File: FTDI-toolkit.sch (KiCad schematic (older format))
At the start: 122 parts, among them IC1 TLV70033, IC13 74HC00BQ, IC15 TS5A3359, IC2 TLV70018, IC3 TS5A3359, J1 12401598E4_2A, J2 2X05, J3 2X08, J6 61300411121, Q1 NX3008CBKV, Q2 NX3008CBKV, SW1_A1 1X03, SW1_B1 1X03, SW2_A1 1X03, SW2_B1 1X03, U1 FT2232H-56Q, U10 74LVC2T45GT, U11 NTS0302JKZ, U2 SN74LVC1T45DRLR, U3 SN74LVC1T45DRLR, U4 TXB0104RUT, U5 74LVC2T45GT, U6 74LVC2T45GT, U7 74LVC2T45GT, U8 SN74LVC1T45DRLR, U9 SN74LVC1T45DRLR, Y1 ASFLMB-12.000MHZ-LC-T

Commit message: Move separation resistors for SWD and I2C switches
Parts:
- added C16, C34, C35: C_100n_0402_16V, antmicro-footprints:0402-cap, symbol antmicroCapacitors0402:C_100n_0402_16V
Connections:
- wire segments 482 -> 480
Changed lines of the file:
@@
 Wire Wire Line
 	2200 5800 2200 5750
-Connection ~ 2200 5750
-Wire Wire Line
-	2200 5750 2550 5750
 Wire Wire Line
 	5400 9000 6300 9000
@@
 Text GLabel 5500 3750 1    50   Input ~ 0
 5V_USB
-Connection ~ 2550 5750
 Wire Wire Line
 	2950 9400 3800 9400
@@
 $EndComp
 Wire Wire Line
-	2550 5750 3550 5750
+	2550 5750 2900 5750
 Wire Wire Line
 	2550 6550 2550 6450
@@
 U 1 1 61826E03
 P 14050 13000
-F 0 "U7" H 13800 13400 60  0000 C CNN
-F 1 "74LVC2T45GT" H 14050 13300 60  0000 C CNN
+F 0 "U7" H 13700 13450 60  0000 C CNN
+F 1 "74LVC2T45GT" H 13950 13350 60  0000 C CNN
 F 2 "antmicro-footprints:PSON50P100X195X50-8N" H 14250 13200 60  0001 L CNN
 F 3 "http://www.farnell.com/datasheets/2787504.pdf" H 14250 13300 60  0001 L CNN
@@
 Wire Wire Line
 	13200 10250 13950 10250
-Text GLabel 13450 12750 0    50   Input ~ 0
-3V3_FT
 Wire Wire Line
-	13450 12750 13550 12750
+	13450 12700 13550 12700
 Wire Wire Line
-	13550 12750 13550 12900
+	13550 12700 13550 12900
 Wire Wire Line
 	13550 13200 13750 13200
@@
 BDBUS1
 Wire Wire Line
-	14600 13100 14600 13500
+	14650 13100 14650 13500
 Wire Wire Line
-	14600 13500 13950 13500
-Wire Wire Line
-	14350 13100 14600 13100
+	14350 13100 14650 13100
 Text Label 13500 13500 2    60   ~ 0
 BDBUS2
 Wire Wire Line
-	14350 13000 14600 13000
-Wire Wire Line
 	14800 13100 14800 12900
 Wire Wire Line
 	14800 13100 15350 13100
 Wire Wire Line
-	14600 12750 13650 12750
+	14650 12700 13650 12700
 Wire Wire Line
-	13650 12750 13650 13100
+	13650 12700 13650 13100
 Wire Wire Line
-	14600 13000 14600 12750
-Connection ~ 14600 13000
+	14650 13000 14650 12700
 Wire Wire Line
-	14600 13000 15550 13000
+	14650 13000 15550 13000
 $Comp
 L antmicroCapacitors0402:C_100n_0402_16V C31
@@
 L antmicroResistors0402:R_510_0402 R28
 U 1 1 620B794C
-P 13800 13500
-F 0 "R28" H 13900 13300 60  0000 L CNN
-F 1 "R_510_0402" H 13800 13350 60  0001 C CNN
-F 2 "antmicro-footprints:0402-res" H 14000 13700 60  0001 L CNN
-F 3 "" H 13800 13500 50  0001 C CNN
-F 4 "Vishay" H 14000 13900 60  0001 L CNN "Manufacturer"
-F 5 "CRCW0402510RFKEDC" H 14000 13800 60  0001 L CNN "MPN"
-F 6 "510R" H 13850 13400 50  0000 L CNN "Val"
-	1    13800 13500
+P 14500 13000
+F 0 "R28" H 14400 12750 60  0000 L CNN
+F 1 "R_510_0402" H 14500 12850 60  0001 C CNN
+F 2 "antmicro-footprints:0402-res" H 14700 13200 60  0001 L CNN
+F 3 "" H 14500 13000 50  0001 C CNN
+F 4 "Vishay" H 14700 13400 60  0001 L CNN "Manufacturer"
+F 5 "CRCW0402510RFKEDC" H 14700 13300 60  0001 L CNN "MPN"
+F 6 "510R" H 14400 12850 50  0000 L CNN "Val"
+	1    14500 13000
 	-1   0    0    1
 $EndComp
-Wire Wire Line
-	13650 13500 13150 13500
 $Comp
 L antmicroResistors0402:R_220R_0402 R35
@@
 U 1 1 62439B48
 P 10850 14550
-F 0 "U6" H 10600 14950 60  0000 C CNN
-F 1 "74LVC2T45GT" H 10850 14850 60  0000 C CNN
+F 0 "U6" H 10350 15000 60  0000 C CNN
+F 1 "74LVC2T45GT" H 10600 14900 60  0000 C CNN
 F 2 "antmicro-footprints:PSON50P100X195X50-8N" H 11050 14750 60  0001 L CNN
 F 3 "http://www.farnell.com/datasheets/2787504.pdf" H 11050 14850 60  0001 L CNN
@@
 	1    0    0    -1
 $EndComp
-Wire Wire Line
-	10750 14500 10700 14500
 Text GLabel 10250 14300 0    50   Input ~ 0
 3V3_FT
@@
 Text Label 9950 14650 2    60   ~ 0
 ADBUS3
-Wire Wire Line
-	11400 15050 10300 15050
 Text Label 9950 15050 2    60   ~ 0
 ADBUS2
@@
 	11150 14550 11400 14550
 Wire Wire Line
-	11400 14300 10450 14300
-Wire Wire Line
 	10450 14300 10450 14650
 $Comp
 L antmicroResistors0402:R_510_0402 R19
 U 1 1 62439B6B
-P 10150 15050
-F 0 "R19" H 10200 14950 60  0000 L CNN
-F 1 "R_510_0402" H 10150 14900 60  0001 C CNN
-F 2 "antmicro-footprints:0402-res" H 10350 15250 60  0001 L CNN
-F 3 "" H 10150 15050 50  0001 C CNN
-F 4 "Vishay" H 10350 15450 60  0001 L CNN "Manufacturer"
-F 5 "CRCW0402510RFKEDC" H 10350 15350 60  0001 L CNN "MPN"
-F 6 "510R" H 9950 14950 50  0000 L CNN "Val"
-	1    10150 15050
+P 11250 14300
+F 0 "R19" H 11300 14200 60  0000 L CNN
+F 1 "R_510_0402" H 11250 14150 60  0001 C CNN
+F 2 "antmicro-footprints:0402-res" H 11450 14500 60  0001 L CNN
+F 3 "" H 11250 14300 50  0001 C CNN
+F 4 "Vishay" H 11450 14700 60  0001 L CNN "Manufacturer"
+F 5 "CRCW0402510RFKEDC" H 11450 14600 60  0001 L CNN "MPN"
+F 6 "510R" H 11050 14200 50  0000 L CNN "Val"
+	1    11250 14300
 	-1   0    0    1
 $EndComp
 Wire Wire Line
-	10000 15050 9600 15050
-Wire Wire Line
 	11400 14550 11400 14300
 Wire Wire Line
@@
 U 1 1 627031C0
 P 10150 14650
-F 0 "R13" H 10050 14550 60  0000 C CNN
+F 0 "R13" H 10000 14550 60  0000 C CNN
 F 1 "R_220R_0402" H 10150 14500 60  0001 C CNN
 F 2 "antmicro-footprints:0402-res" H 10350 14850 60  0001 L CNN
@@
 F 4 "Panasonic" H 10350 15050 60  0001 L CNN "Manufacturer"
 F 5 "ERJ2GEJ221X" H 10350 14950 60  0001 L CNN "MPN"
-F 6 "220R" H 10250 14550 50  0000 C CNN "Val"
+F 6 "220R" H 10200 14550 50  0000 C CNN "Val"
 	1    10150 14650
 	1    0    0    -1
@@
 Wire Wire Line
 	10100 11750 10650 11750
+Text GLabel 11850 8400 1    50   Input ~ 0
+VCCIOA
+$Comp
+L antmicroCapacitors0402:C_100n_0402_16V C35
+U 1 1 5F8AD051
+P 11850 8550
+F 0 "C35" H 11965 8595 60  0000 L CNN
+F 1 "C_100n_0402_16V" H 11850 8400 60  0001 C CNN
+F 2 "antmicro-footprints:0402-cap" H 12050 8750 60  0001 L CNN
+F 3 "" H 11850 8550 50  0001 C CNN
+F 4 "MULTICOMP" H 12050 8950 60  0001 L CNN "Manufacturer"
+F 5 "MC0402B104K160CT" H 12050 8850 60  0001 L CNN "MPN"
+F 6 "100n" H 11950 8700 50  0000 L CNN "Val"
+	1    11850 8550
+	-1   0    0    1
+$EndComp
+$Comp
+L power:GND #PWR035
+U 1 1 5F8AD057
+P 11850 8700
+F 0 "#PWR035" H 11850 8450 50  0001 C CNN
+F 1 "GND" H 11855 8527 50  0000 C CNN
+F 2 "" H 11850 8700 50  0001 C CNN
+F 3 "" H 11850 8700 50  0001 C CNN
+	1    11850 8700
+	1    0    0    -1
+$EndComp
+Connection ~ 2550 5750
+Connection ~ 2200 5750
+Wire Wire Line
+	2200 5750 2550 5750
+$Comp
+L antmicroCapacitors0402:C_100n_0402_16V C16
+U 1 1 5F9553AE
+P 2900 5950
+F 0 "C16" H 3050 6050 60  0000 C CNN
+F 1 "C_100n_0402_16V" H 2900 5800 60  0001 C CNN
+F 2 "antmicro-footprints:0402-cap" H 3100 6150 60  0001 L CNN
+F 3 "" H 2900 5950 50  0001 C CNN
+F 4 "MULTICOMP" H 3100 6350 60  0001 L CNN "Manufacturer"
+F 5 "MC0402B104K160CT" H 3100 6250 60  0001 L CNN "MPN"
+F 6 "100n" H 3050 5850 50  0000 C CNN "Val"
+	1    2900 5950
+	1    0    0    1
+$EndComp
+$Comp
+L power:GND #PWR017
+U 1 1 5F9553B4
+P 2900 6100
+F 0 "#PWR017" H 2900 5850 50  0001 C CNN
+F 1 "GND" H 2905 5927 50  0000 C CNN
+F 2 "" H 2900 6100 50  0001 C CNN
+F 3 "" H 2900 6100 50  0001 C CNN
+	1    2900 6100
+	1    0    0    -1
+$EndComp
+Wire Wire Line
+	2900 5800 2900 5750
+Connection ~ 2900 5750
+Wire Wire Line
+	2900 5750 3550 5750
+Text GLabel 9250 8400 1    50   Input ~ 0
+3V3_FT
+$Comp
+L antmicroCapacitors0402:C_100n_0402_16V C34
+U 1 1 5FA84652
+P 9250 8550
+F 0 "C34" H 9365 8595 60  0000 L CNN
+F 1 "C_100n_0402_16V" H 9250 8400 60  0001 C CNN
+F 2 "antmicro-footprints:0402-cap" H 9450 8750 60  0001 L CNN
+F 3 "" H 9250 8550 50  0001 C CNN
+F 4 "MULTICOMP" H 9450 8950 60  0001 L CNN "Manufacturer"
+F 5 "MC0402B104K160CT" H 9450 8850 60  0001 L CNN "MPN"
+F 6 "100n" H 9350 8700 50  0000 L CNN "Val"
+	1    9250 8550
+	-1   0    0    1
+$EndComp
+$Comp
+L power:GND #PWR034
+U 1 1 5FA84658
+P 9250 8700
+F 0 "#PWR034" H 9250 8450 50  0001 C CNN
+F 1 "GND" H 9255 8527 50  0000 C CNN
+F 2 "" H 9250 8700 50  0001 C CNN
+F 3 "" H 9250 8700 50  0001 C CNN
+	1    9250 8700
+	1    0    0    -1
+$EndComp
+Wire Wire Line
+	9600 15050 11400 15050
+Wire Wire Line
+	11100 14300 10450 14300
+Wire Wire Line
+	13150 13500 14650 13500
+Connection ~ 14650 13000
+Text GLabel 13450 12700 0    50   Input ~ 0
+3V3_FT
 $EndSCHEMATC

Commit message: Update silk-screen markings
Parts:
- U10, U5, U6, U7: symbol antmicroLogicTranslatorsLevelShifters:74LVC2T45GT -> FTDI-toolkit-rescue:74LVC2T45GT-antmicroLogicTranslatorsLevelShifters
- U11: symbol antmicroLogicTranslatorsLevelShifters:NTS0302JKZ -> FTDI-toolkit-rescue:NTS0302JKZ-antmicroLogicTranslatorsLevelShifters
- U2, U3, U8, U9: symbol antmicroLogicTranslatorsLevelShifters:SN74LVC1T45DRLR -> FTDI-toolkit-rescue:SN74LVC1T45DRLR-antmicroLogicTranslatorsLevelShifters
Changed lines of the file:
@@
 Auxillary connector
 $Comp
-L antmicroLogicTranslatorsLevelShifters:NTS0302JKZ U11
+L FTDI-toolkit-rescue:NTS0302JKZ-antmicroLogicTranslatorsLevelShifters U11
 U 1 1 5F68E14C
 P 15950 13050
@@
 $EndComp
 $Comp
-L antmicroLogicTranslatorsLevelShifters:SN74LVC1T45DRLR U2
+L FTDI-toolkit-rescue:SN74LVC1T45DRLR-antmicroLogicTranslatorsLevelShifters U2
 U 1 1 5F68EFE9
 P 10700 9500
@@
 $EndComp
 $Comp
-L antmicroLogicTranslatorsLevelShifters:SN74LVC1T45DRLR U3
+L FTDI-toolkit-rescue:SN74LVC1T45DRLR-antmicroLogicTranslatorsLevelShifters U3
 U 1 1 5FA4FA1B
 P 10750 10250
@@
 nMPSSE_A
 $Comp
-L antmicroLogicTranslatorsLevelShifters:74LVC2T45GT U5
+L FTDI-toolkit-rescue:74LVC2T45GT-antmicroLogicTranslatorsLevelShifters U5
 U 1 1 5FB5368D
 P 10750 10950
@@
 $EndComp
 $Comp
-L antmicroLogicTranslatorsLevelShifters:SN74LVC1T45DRLR U8
+L FTDI-toolkit-rescue:SN74LVC1T45DRLR-antmicroLogicTranslatorsLevelShifters U8
 U 1 1 5FCE022B
 P 14250 9500
@@
 $EndComp
 $Comp
-L antmicroLogicTranslatorsLevelShifters:SN74LVC1T45DRLR U9
+L FTDI-toolkit-rescue:SN74LVC1T45DRLR-antmicroLogicTranslatorsLevelShifters U9
 U 1 1 5FCE0248
 P 14250 10250
@@
 nMPSSE_B
 $Comp
-L antmicroLogicTranslatorsLevelShifters:74LVC2T45GT U10
+L FTDI-toolkit-rescue:74LVC2T45GT-antmicroLogicTranslatorsLevelShifters U10
 U 1 1 5FCE025B
 P 14250 10950
@@
 Connection ~ 15500 12300
 $Comp
-L antmicroLogicTranslatorsLevelShifters:74LVC2T45GT U7
+L FTDI-toolkit-rescue:74LVC2T45GT-antmicroLogicTranslatorsLevelShifters U7
 U 1 1 61826E03
 P 14050 13000
@@
 	17100 12300 17350 12300
 $Comp
-L antmicroLogicTranslatorsLevelShifters:74LVC2T45GT U6
+L FTDI-toolkit-rescue:74LVC2T45GT-antmicroLogicTranslatorsLevelShifters U6
 U 1 1 62439B48
 P 10850 14550

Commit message: Bump revision to 1.2.1
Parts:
- 1V8_A1, 1V8_B1, 3V3_A1, 3V3_B1, 5V0_A1, 5V0_B1, RX_A1, RX_B1, TX_A1, TX_B1, USB1: footprint antmicro-footprints:LED_0603 -> FTDI-toolkit-footprints:LED_0603; symbol antmicroLEDIndicationDiscrete:LG_L29K-G2J1-24-Z -> FTDI-toolkit:LG_L29K-G2J1-24-Z
- C1, C2, C5, C6: footprint antmicro-footprints:0603-cap -> FTDI-toolkit-footprints:0603-cap; symbol antmicroCapacitors0603:C_1u_0603 -> FTDI-toolkit:C_1u_0603
- C10, C12, C13, C14, C15, C16, C17, C18, C19, C20, C21, C22, C24, C25, C26, C28, C29, C30, C31, C32, C33, C34, C35, C4, C7, C8, C9: footprint antmicro-footprints:0402-cap -> FTDI-toolkit-footprints:0402-cap; symbol antmicroCapacitors0402:C_100n_0402_16V -> FTDI-toolkit:C_100n_0402_16V
- C11, C23, C27: footprint antmicro-footprints:0402-cap -> FTDI-toolkit-footprints:0402-cap; symbol antmicroCapacitors0402:C_4u7_0402 -> FTDI-toolkit:C_4u7_0402
- C3: footprint antmicro-footprints:0402-cap -> FTDI-toolkit-footprints:0402-cap; symbol antmicroCapacitors0402:C_10n_0402 -> FTDI-toolkit:C_10n_0402
- D1: footprint antmicro-footprints:SOT-3 -> FTDI-toolkit-footprints:SOT-3; symbol antmicroTVSDiodes:TPD2E009 -> FTDI-toolkit:TPD2E009
- D2: footprint antmicro-footprints:TPD6E05U06 -> FTDI-toolkit-footprints:TPD6E05U06; symbol antmicroTVSDiodes:TPD6E05U06 -> FTDI-toolkit:TPD6E05U06
- D3: footprint antmicro-footprints:SOD-523 -> FTDI-toolkit-footprints:SOD-523; symbol antmicroDiodesRectifiersSingle:BAT54-02V-V-G -> FTDI-toolkit:BAT54-02V-V-G
- FB1, FB2: footprint antmicro-footprints:0402-res -> FTDI-toolkit-footprints:0402-res; symbol antmicroFerriteBeadsandChips:BLM15AG601SN1D -> FTDI-toolkit:BLM15AG601SN1D
- IC1: footprint antmicro-footprints:SC-70-5 -> FTDI-toolkit-footprints:SC-70-5; symbol antmicroPMICVoltageRegulatorsLinear:TLV70033 -> FTDI-toolkit:TLV70033
- IC13: footprint antmicro-footprints:DHVQFN14 -> FTDI-toolkit-footprints:DHVQFN14; symbol antmicroLogicGatesandInverters:74HC00BQ -> FTDI-toolkit:74HC00BQ
- IC15, IC3: footprint antmicro-footprints:TS5A3359 -> FTDI-toolkit-footprints:TS5A3359; symbol antmicroInterfaceAnalogSwitchesMultiplexersDemultiplexers:TS5A3359 -> FTDI-toolkit:TS5A3359
- IC2: footprint antmicro-footprints:SC-70-5 -> FTDI-toolkit-footprints:SC-70-5; symbol antmicroPMICVoltageRegulatorsLinear:TLV70018 -> FTDI-toolkit:TLV70018
- J1: footprint antmicro-footprints:USB-C_Female_12401X -> FTDI-toolkit-footprints:USB-C_Female_12401X; symbol antmicroUSBDVIHDMIConnectors:12401598E4_2A -> FTDI-toolkit:12401598E4_2A
- J2: footprint antmicro-footprints:SHF-105-01-X-D-SM -> FTDI-toolkit-footprints:SHF-105-01-X-D-SM; symbol antmicroRectangularConnectorsHeadersMalePins:2X05 -> FTDI-toolkit:2X05
- J3: footprint antmicro-footprints:MH_2X08_2.54_RA -> FTDI-toolkit-footprints:MH_2X08_2.54_RA; symbol antmicroRectangularConnectorsHeadersMalePins:2X08 -> FTDI-toolkit:2X08
- J6: footprint antmicro-footprints:PinHeader_1x4_P2.54mm_Drill1.02mm -> FTDI-toolkit-footprints:PinHeader_1x4_P2.54mm_Drill1.02mm; symbol antmicroRectangularConnectorsHeadersMalePins:61300411121 -> FTDI-toolkit:61300411121
- L1, L2: footprint antmicro-footprints:0603-res -> FTDI-toolkit-footprints:0603-res; symbol antmicroFerriteBeadsandChips:BLM18PG121SN1D -> FTDI-toolkit:BLM18PG121SN1D
- N1: footprint antmicro-footprints:antmicro-logo_scaled_12mm -> FTDI-toolkit-footprints:antmicro-logo_scaled_12mm; symbol antmicroMechanicalParts:antmicro_logo -> FTDI-toolkit:antmicro_logo
- N2: footprint antmicro-footprints:OSHW-Logo2_7.3x6mm_SilkScreen -> FTDI-toolkit-footprints:OSHW-Logo2_7.3x6mm_SilkScreen; symbol antmicroMechanicalParts:oshw_logo -> FTDI-toolkit:oshw_logo
- Q1, Q2: footprint antmicro-footprints:SOT-666 -> FTDI-toolkit-footprints:SOT-666; symbol antmicroTransistorsFETsMOSFETsArrays:NX3008CBKV -> FTDI-toolkit:NX3008CBKV
- R1, R11, R12, R13, R14, R15, R18, R3, R34, R35, R36, R6, R7, R8: footprint antmicro-footprints:0402-res -> FTDI-toolkit-footprints:0402-res; symbol antmicroResistors0402:R_220R_0402 -> FTDI-toolkit:R_220R_0402
- R10: footprint antmicro-footprints:0603-res -> FTDI-toolkit-footprints:0603-res; symbol antmicroResistors0603:R_0R_0603 -> FTDI-toolkit:R_0R_0603
- R16, R17, R22, R24, R25, R26, R27, R30, R32, R33, R4, R5: footprint antmicro-footprints:0402-res -> FTDI-toolkit-footprints:0402-res; symbol antmicroResistors0402:R_10k_0402 -> FTDI-toolkit:R_10k_0402
- R19, R28: footprint antmicro-footprints:0402-res -> FTDI-toolkit-footprints:0402-res; symbol antmicroResistors0402:R_510_0402 -> FTDI-toolkit:R_510_0402
- R2: footprint antmicro-footprints:0402-res -> FTDI-toolkit-footprints:0402-res; symbol antmicroResistors0402:R_470R_0402 -> FTDI-toolkit:R_470R_0402
- R20, R23, R29: footprint antmicro-footprints:0402-res -> FTDI-toolkit-footprints:0402-res; symbol antmicroResistors0402:R_56k_0402 -> FTDI-toolkit:R_56k_0402
- R21: footprint antmicro-footprints:0402-res -> FTDI-toolkit-footprints:0402-res; symbol antmicroResistors0402:R_4k7_0402 -> FTDI-toolkit:R_4k7_0402
- R9: footprint antmicro-footprints:0402-res -> FTDI-toolkit-footprints:0402-res; symbol antmicroResistors0402:R_12k_0402 -> FTDI-toolkit:R_12k_0402
- SW1_A1, SW1_B1, SW2_A1, SW2_B1: footprint antmicro-footprints:MH_1X03_2.54 -> FTDI-toolkit-footprints:MH_1X03_2.54; symbol antmicroRectangularConnectorsHeadersMalePins:1X03 -> FTDI-toolkit:1X03
- TP1, TP2, TP3, TP4, TP5, TP6, TP7, TP8: footprint antmicro-footprints:Testpoint_smd_0_75mm -> FTDI-toolkit-footprints:Testpoint_smd_0_75mm; symbol antmicroTestPoints:TP_SMD_0_75MM -> FTDI-toolkit:TP_SMD_0_75MM
- U1: footprint antmicro-footprints:QFN-56-1EP_8x8mm_P0.5mm_EP5.5.9x5.9mm -> FTDI-toolkit-footprints:QFN-56-1EP_8x8mm_P0.5mm_EP5.5.9x5.9mm; symbol antmicroInterfaceControllers:FT2232H-56Q -> FTDI-toolkit:FT2232H-56Q
- U10, U5, U6, U7: footprint antmicro-footprints:PSON50P100X195X50-8N -> FTDI-toolkit-footprints:PSON50P100X195X50-8N; symbol FTDI-toolkit-rescue:74LVC2T45GT-antmicroLogicTranslatorsLevelShifters -> FTDI-toolkit:74LVC2T45GT-antmicroLogicTranslatorsLevelShifters
- U11: footprint antmicro-footprints:X2SON8 -> FTDI-toolkit-footprints:X2SON8; symbol FTDI-toolkit-rescue:NTS0302JKZ-antmicroLogicTranslatorsLevelShifters -> FTDI-toolkit:NTS0302JKZ-antmicroLogicTranslatorsLevelShifters
- U2, U3, U8, U9: footprint antmicro-footprints:SOT-553-6 -> FTDI-toolkit-footprints:SOT-553-6; symbol FTDI-toolkit-rescue:SN74LVC1T45DRLR-antmicroLogicTranslatorsLevelShifters -> FTDI-toolkit:SN74LVC1T45DRLR-antmicroLogicTranslatorsLevelShifters
- U4: footprint Package_DFN_QFN:Texas_R_PUQFN-N12 -> FTDI-toolkit-footprints:Texas_R_PUQFN-N12; symbol antmicroLogicTranslatorsLevelShifters:TXB0104RUT -> FTDI-toolkit:TXB0104RUT
- Y1: footprint antmicro-footprints:ASFLMB -> FTDI-toolkit-footprints:ASFLMB; symbol antmicroOscillators:ASFLMB-12.000MHZ-LC-T -> FTDI-toolkit:ASFLMB-12.000MHZ-LC-T
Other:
- note removed: "https://dev.antmicro.com/git/antmicro-ftdi-toolkit-hw"

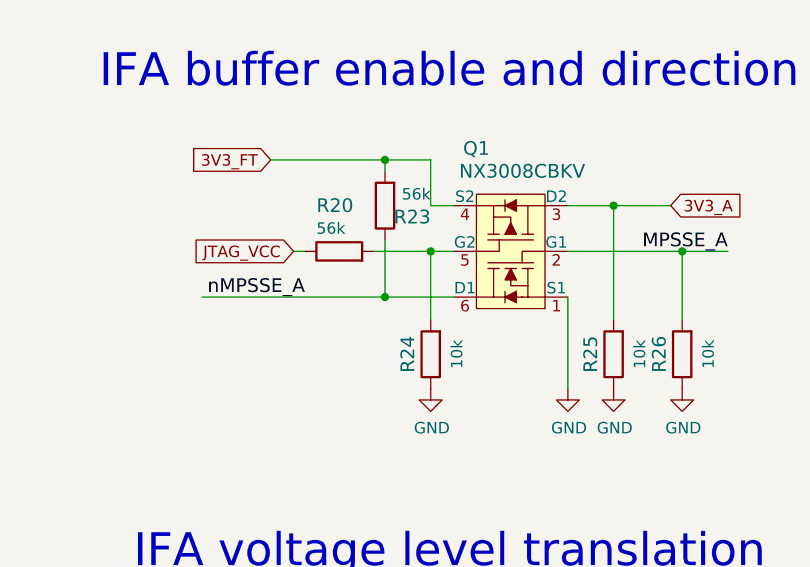
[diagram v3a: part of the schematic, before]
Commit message: Replaced R20, R24 with 4k7 and 56k respectively. Changes corrected on sch and pcb
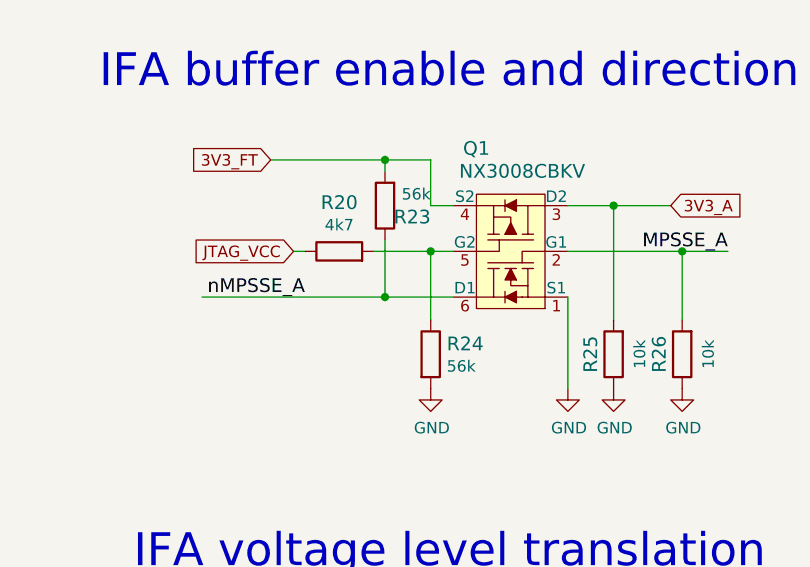
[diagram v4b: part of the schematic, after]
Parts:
- removed R20: R_56k_0402, FTDI-toolkit-footprints:0402-res, symbol FTDI-toolkit:R_56k_0402
- removed R24: R_10k_0402, FTDI-toolkit-footprints:0402-res, symbol FTDI-toolkit:R_10k_0402
- added R20: R_4k7_0402, FTDI-toolkit-footprints:0402-res, symbol antmicroResistors0402:R_4k7_0402
- added R24: R_56k_0402, FTDI-toolkit-footprints:0402-res, symbol antmicroResistors0402:R_56k_0402
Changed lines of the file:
@@
 	0    -1   -1   0
 $EndComp
-$Comp
-L FTDI-toolkit:R_10k_0402 R24
-U 1 1 603C712C
-P 10800 6950
-F 0 "R24" H 10800 7050 60  0000 C CNN
-F 1 "R_10k_0402" H 10800 6800 60  0001 C CNN
-F 2 "FTDI-toolkit-footprints:0402-res" H 11000 7150 60  0001 L CNN
-F 3 "" H 10800 6950 50  0001 C CNN
-F 4 "VISHAY" H 11000 7350 60  0001 L CNN "Manufacturer"
-F 5 "CRCW040210K0FKEDHP" H 11000 7250 60  0001 L CNN "MPN"
-F 6 "10k" H 10800 6835 50  0000 C CNN "Val"
-	1    10800 6950
-	0    -1   -1   0
-$EndComp
 Text GLabel 10100 6100 0    50   Input ~ 0
 3V3_FT
@@
 nMPSSE_A
 $Comp
-L FTDI-toolkit:R_56k_0402 R20
-U 1 1 60639AEC
-P 10400 6500
-F 0 "R20" H 10300 6700 60  0000 L CNN
-F 1 "R_56k_0402" H 10400 6350 60  0001 C CNN
-F 2 "FTDI-toolkit-footprints:0402-res" H 10600 6700 60  0001 L CNN
-F 3 "" H 10400 6500 50  0001 C CNN
-F 4 "VISHAY" H 10600 6900 60  0001 L CNN "Manufacturer"
-F 5 "CRCW040256K0FKED" H 10600 6800 60  0001 L CNN "MPN"
-F 6 "56k" H 10300 6600 50  0000 L CNN "Val"
-	1    10400 6500
-	1    0    0    -1
-$EndComp
-$Comp
 L FTDI-toolkit:GND #PWR09
 U 1 1 606C9DB8
@@
 EndData
 $EndBitmap
+$Comp
+L antmicroResistors0402:R_56k_0402 R24
+U 1 1 62526A39
+P 10800 6950
+F 0 "R24" V 10755 7020 60  0000 L CNN
+F 1 "R_56k_0402" H 10800 6800 60  0001 C CNN
+F 2 "FTDI-toolkit-footprints:0402-res" H 11000 7150 60  0001 L CNN
+F 3 "" H 10800 6950 50  0001 C CNN
+F 4 "VISHAY" H 11000 7350 60  0001 L CNN "Manufacturer"
+F 5 "CRCW040256K0FKED" H 11000 7250 60  0001 L CNN "MPN"
+F 6 "56k" V 10853 7020 50  0000 L CNN "Val"
+	1    10800 6950
+	0    1    1    0
+$EndComp
+$Comp
+L antmicroResistors0402:R_4k7_0402 R20
+U 1 1 62579236
+P 10400 6500
+F 0 "R20" H 10400 6713 60  0000 C CNN
+F 1 "R_4k7_0402" H 10400 6350 60  0001 C CNN
+F 2 "FTDI-toolkit-footprints:0402-res" H 10600 6700 60  0001 L CNN
+F 3 "" H 10400 6500 50  0001 C CNN
+F 4 "VISHAY" H 10600 6900 60  0001 L CNN "Manufacturer"
+F 5 "MCS04020C4701FE000" H 10600 6800 60  0001 L CNN "MPN"
+F 6 "4k7" H 10400 6615 50  0000 C CNN "Val"
+	1    10400 6500
+	1    0    0    -1
+$EndComp
 $EndSCHEMATC
